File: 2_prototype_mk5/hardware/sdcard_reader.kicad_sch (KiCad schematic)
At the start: 4 parts, among them J1 Micro_SD_Card

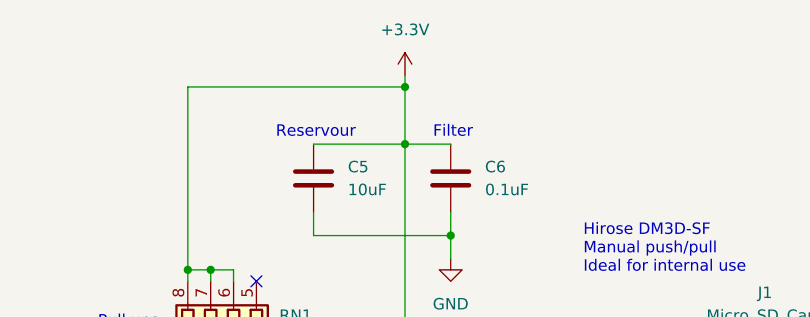
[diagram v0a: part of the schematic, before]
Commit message: Major MKV redesign using embedded RP2350
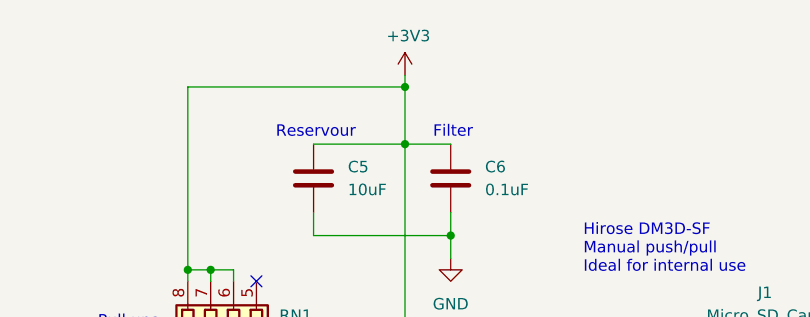
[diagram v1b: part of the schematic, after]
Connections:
- net +3.3V renamed +3V3
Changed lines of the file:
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@@
 		(dnp no)
 		(fields_autoplaced yes)
-		(property "Reference" "#PWR027"
+		(property "Reference" "#PWR011"
 			(at 107.95 120.65 0)
 			(hide yes)
@@
 			(project "HDD Synth Prototype MK5"
 				(path "/1a22431a-ba36-40a0-9a7e-c2a82ec69c53/d1519e40-91bf-450d-a5bd-0730e6716e0a"
-					(reference "#PWR027")
+					(reference "#PWR011")
 					(unit 1)
 				)
@@
 		(dnp no)
 		(fields_autoplaced yes)
-		(property "Reference" "#PWR035"
+		(property "Reference" "#PWR012"
 			(at 113.03 76.2 0)
 			(hide yes)
@@
 			(project "HDD Synth Prototype MK5"
 				(path "/1a22431a-ba36-40a0-9a7e-c2a82ec69c53/d1519e40-91bf-450d-a5bd-0730e6716e0a"
-					(reference "#PWR035")
+					(reference "#PWR012")
 					(unit 1)
 				)
@@
 	)
 	(symbol
-		(lib_id "power:+3.3V")
+		(lib_id "power:+3V3")
 		(at 107.95 49.53 0)
 		(unit 1)
@@
 		(in_pos_files yes)
 		(dnp no)
-		(fields_autoplaced yes)
-		(property "Reference" "#PWR015"
+		(property "Reference" "#PWR058"
 			(at 107.95 53.34 0)
 			(hide yes)
@@
 			)
 		)
-		(property "Value" "+3.3V"
-			(at 107.95 44.45 0)
+		(property "Value" "+3V3"
+			(at 108.331 45.1358 0)
 			(show_name no)
 			(do_not_autoplace no)
@@
 			)
 		)
-		(property "Description" "Power symbol creates a global label with name \"+3.3V\""
+		(property "Description" ""
 			(at 107.95 49.53 0)
-			(hide yes)
 			(show_name no)
 			(do_not_autoplace no)
@@
 			(project "HDD Synth Prototype MK5"
 				(path "/1a22431a-ba36-40a0-9a7e-c2a82ec69c53/d1519e40-91bf-450d-a5bd-0730e6716e0a"
-					(reference "#PWR015")
-					(unit 1)
-				)
-			)
-			(project ""
-				(path "/5a2f0aa7-670f-4d0d-8d56-ad98c847383a/e22d441a-90fa-476a-aba2-429f624bfc45"
-					(reference "#PWR015")
-					(unit 1)
-				)
-			)
-			(project "FDD Synth prototype MK1"
-				(path "/ed113b11-1722-4efb-9669-9e8c19f5c8fd/fe112bae-5f2b-4222-b0d9-22039210278c"
-					(reference "#PWR015")
-					(unit 1)
-				)
+					(reference "#PWR058")
+					(unit 1)
+				)

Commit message: MKV: Add LCSC numbers and resolve DRC errors
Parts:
- C5: LCSC_Part_Number (none) -> C13585
- C6: LCSC_Part_Number (none) -> C14663
